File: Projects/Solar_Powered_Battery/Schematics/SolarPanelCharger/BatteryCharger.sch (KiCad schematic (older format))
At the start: 17 parts, among them J2 Conn_01x05_Female, Q3 BC847, U4 TP4056

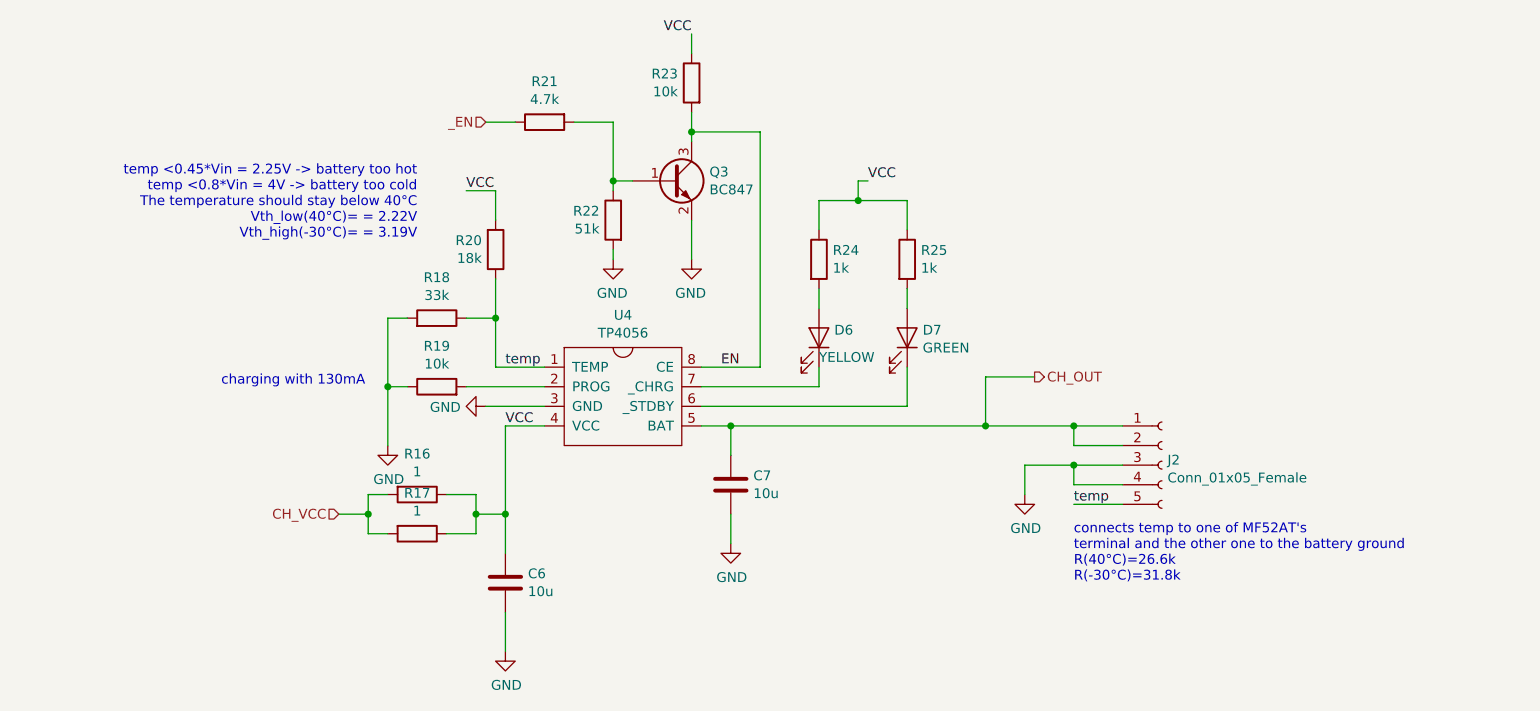
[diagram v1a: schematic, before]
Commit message: make modifications to the solar charger circuit
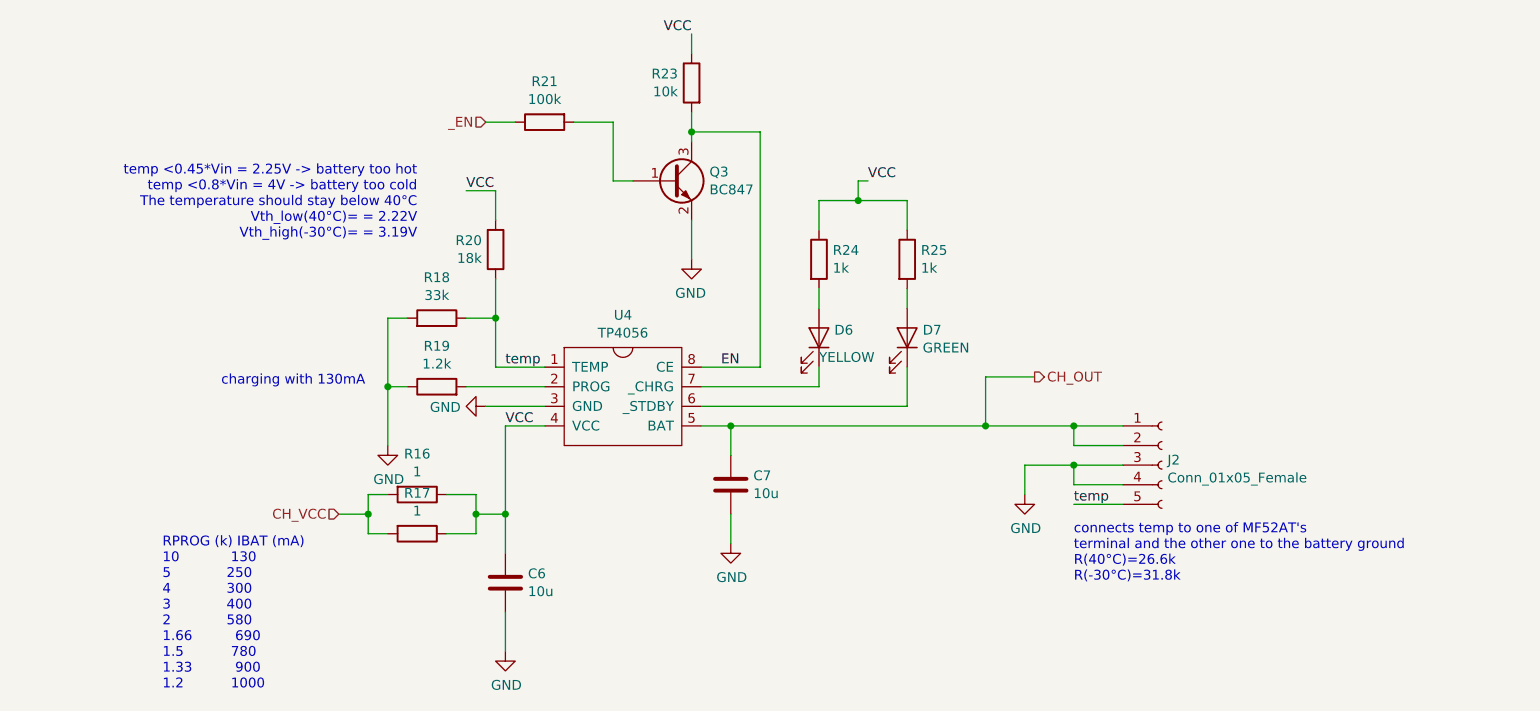
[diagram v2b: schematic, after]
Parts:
- removed R22: 51k, Resistor_SMD:R_0603_1608Metric_Pad1.05x0.95mm_HandSolder, symbol Device:R
- R19: value 10k -> 1.2k
- R21: value 4.7k -> 100k
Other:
- note added: "RPROG (k) IBAT (mA)\n10 130\n5 250\n4 300\n3 400\n2 580\n1.66 690\n1.5 780\n1.33 900\n1.2 1000"
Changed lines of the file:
@@
 P 3800 3500
 F 0 "R19" V 4007 3500 50  0000 C CNN
-F 1 "10k" V 3916 3500 50  0000 C CNN
+F 1 "1.2k" V 3916 3500 50  0000 C CNN
 F 2 "Resistor_SMD:R_0603_1608Metric_Pad1.05x0.95mm_HandSolder" V 3730 3500 50  0001 C CNN
 F 3 "~" H 3800 3500 50  0001 C CNN
@@
 	4800 2450 4700 2450
 Wire Wire Line
-	4700 2500 4700 2450
-$Comp
-L Device:R R22
-U 1 1 5CB3CF2E
-P 4700 2650
-F 0 "R22" H 4770 2696 50  0000 L CNN
-F 1 "51k" H 4770 2605 50  0000 L CNN
-F 2 "Resistor_SMD:R_0603_1608Metric_Pad1.05x0.95mm_HandSolder" V 4630 2650 50  0001 C CNN
-F 3 "~" H 4700 2650 50  0001 C CNN
-	1    4700 2650
-	-1   0    0    -1
-$EndComp
-$Comp
-L power:GND #PWR021
-U 1 1 5CB3EBE6
-P 4700 2850
-F 0 "#PWR021" H 4700 2600 50  0001 C CNN
-F 1 "GND" H 4705 2677 50  0000 C CNN
-F 2 "" H 4700 2850 50  0001 C CNN
-F 3 "" H 4700 2850 50  0001 C CNN
-	1    4700 2850
-	-1   0    0    -1
-$EndComp
-Wire Wire Line
-	4700 2800 4700 2850
-Wire Wire Line
 	5100 2200 5450 2200
 Connection ~ 5100 2200
@@
 P 4350 2150
 F 0 "R21" V 4143 2150 50  0000 C CNN
-F 1 "4.7k" V 4234 2150 50  0000 C CNN
+F 1 "100k" V 4234 2150 50  0000 C CNN
 F 2 "Resistor_SMD:R_0603_1608Metric_Pad1.05x0.95mm_HandSolder" V 4280 2150 50  0001 C CNN
 F 3 "~" H 4350 2150 50  0001 C CNN
@@
 Wire Wire Line
 	4700 2150 4700 2450
-Connection ~ 4700 2450
 Wire Wire Line
 	4200 2150 4050 2150
+Text Notes 2400 5050 0    50   ~ 0
+RPROG (k) IBAT (mA)\n10            130\n5             250\n4             300\n3             400\n2             580\n1.66          690\n1.5           780\n1.33          900\n1.2           1000
 $EndSCHEMATC
